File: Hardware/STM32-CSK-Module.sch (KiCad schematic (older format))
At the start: 0 parts

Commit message: Physical interface layout
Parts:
- added H? (x2): CUBESAT-PSPM, ~, symbol CUBESAT-PSPM
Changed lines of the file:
@@
 LIBS:power
 LIBS:Aerodyne_v2
+LIBS:STM32-CSK-Module-cache
 EELAYER 27 0
 EELAYER END
@@
 Comment4 ""
 $EndDescr
+$Comp
+L CUBESAT-PSPM H?
+U 1 1 547E0580
+P 4400 3500
+F 0 "H?" H 4400 4800 60  0000 C CNN
+F 1 "CUBESAT-PSPM" H 4400 2200 60  0000 C CNN
+F 2 "~" H 4400 4100 60  0000 C CNN
+F 3 "~" H 4400 4100 60  0000 C CNN
+	1    4400 3500
+	1    0    0    -1
+$EndComp
+$Comp
+L CUBESAT-PSPM H?
+U 2 1 547E058F
+P 7000 3500
+F 0 "H?" H 7000 4800 60  0000 C CNN
+F 1 "CUBESAT-PSPM" H 7000 2200 60  0000 C CNN
+F 2 "~" H 7000 4100 60  0000 C CNN
+F 3 "~" H 7000 4100 60  0000 C CNN
+	2    7000 3500
+	1    0    0    -1
+$EndComp
 $EndSCHEMATC

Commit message: Annotation
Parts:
- gave numbers to parts that had none: 1
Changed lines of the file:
@@
 $EndDescr
 $Comp
-L CUBESAT-PSPM H?
+L CUBESAT-PSPM H1
 U 1 1 547E0580
 P 4400 3500
-F 0 "H?" H 4400 4800 60  0000 C CNN
+F 0 "H1" H 4400 4800 60  0000 C CNN
 F 1 "CUBESAT-PSPM" H 4400 2200 60  0000 C CNN
 F 2 "~" H 4400 4100 60  0000 C CNN
@@
 $EndComp
 $Comp
-L CUBESAT-PSPM H?
+L CUBESAT-PSPM H1
 U 2 1 547E058F
 P 7000 3500
-F 0 "H?" H 7000 4800 60  0000 C CNN
+F 0 "H1" H 7000 4800 60  0000 C CNN
 F 1 "CUBESAT-PSPM" H 7000 2200 60  0000 C CNN
 F 2 "~" H 7000 4100 60  0000 C CNN

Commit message: Add MCU
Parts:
- added U1: STM32F4X7V, symbol STM32F4X7V
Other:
- note added: "AN0"
- note added: "AN1"
- note added: "AN10"
- note added: "AN11"
- note added: "AN12"
- note added: "AN13"
- note added: "AN14"
- note added: "AN15"
- note added: "AN2"
- note added: "AN3"
- note added: "AN4"
- note added: "AN5"
- note added: "AN6"
- note added: "AN7"
- note added: "AN8"
- note added: "AN9"
- note added: "INT1"
- note added: "INT2"
- note added: "SCK0"
- note added: "SCK1"
- note added: "SCL1"
- note added: "SCL2"
- note added: "SD0"
- note added: "SDA1"
- note added: "SDA2"
- note added: "SDI0"
- note added: "SDI1"
- note added: "SDO1"
- note added: "URX0"
- note added: "URX1"
- note added: "UTX0"
- note added: "UTX1"
- note added: "~CS_SD"
- note added: "~SS1"
- note added: "~UCTS0"
- note added: "~UCTS1"
- note added: "~URTS0"
- note added: "~URTS1"
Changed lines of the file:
@@
 EELAYER 27 0
 EELAYER END
-$Descr A4 11693 8268
+$Descr A3 16535 11693
 encoding utf-8
 Sheet 1 1
 Title ""
-Date "2 dec 2014"
+Date "5 dec 2014"
 Rev ""
 Comp ""
@@
 	1    0    0    -1
 $EndComp
+$Comp
+L STM32F4X7V U1
+U 1 1 54823604
+P 3150 6600
+F 0 "U1" H 3150 6700 60  0000 C CNN
+F 1 "STM32F4X7V" V 2950 6600 60  0000 R CNN
+F 2 "" H 3550 6600 60  0000 C CNN
+F 3 "" H 3550 6600 60  0000 C CNN
+	1    3150 6600
+	1    0    0    -1
+$EndComp
+$Comp
+L STM32F4X7V U1
+U 2 1 54823613
+P 3850 6600
+F 0 "U1" H 3850 6700 60  0000 C CNN
+F 1 "STM32F4X7V" V 3650 6600 60  0000 R CNN
+F 2 "" H 4250 6600 60  0000 C CNN
+F 3 "" H 4250 6600 60  0000 C CNN
+	2    3850 6600
+	1    0    0    -1
+$EndComp
+$Comp
+L STM32F4X7V U1
+U 3 1 54823622
+P 4550 6600
+F 0 "U1" H 4550 6700 60  0000 C CNN
+F 1 "STM32F4X7V" V 4350 6600 60  0000 R CNN
+F 2 "" H 4950 6600 60  0000 C CNN
+F 3 "" H 4950 6600 60  0000 C CNN
+	3    4550 6600
+	1    0    0    -1
+$EndComp
+$Comp
+L STM32F4X7V U1
+U 4 1 54823631
+P 5250 6600
+F 0 "U1" H 5250 6700 60  0000 C CNN
+F 1 "STM32F4X7V" V 5050 6600 60  0000 R CNN
+F 2 "" H 5650 6600 60  0000 C CNN
+F 3 "" H 5650 6600 60  0000 C CNN
+	4    5250 6600
+	1    0    0    -1
+$EndComp
+$Comp
+L STM32F4X7V U1
+U 5 1 54823640
+P 5950 6600
+F 0 "U1" H 5950 6700 60  0000 C CNN
+F 1 "STM32F4X7V" V 5750 6600 60  0000 R CNN
+F 2 "" H 6350 6600 60  0000 C CNN
+F 3 "" H 6350 6600 60  0000 C CNN
+	5    5950 6600
+	1    0    0    -1
+$EndComp
+$Comp
+L STM32F4X7V U1
+U 6 1 54823663
+P 6650 6600
+F 0 "U1" H 6650 6700 60  0000 C CNN
+F 1 "STM32F4X7V" V 6450 6600 60  0000 R CNN
+F 2 "" H 7050 6600 60  0000 C CNN
+F 3 "" H 7050 6600 60  0000 C CNN
+	6    6650 6600
+	1    0    0    -1
+$EndComp
+$Comp
+L STM32F4X7V U1
+U 7 1 54823677
+P 7350 6600
+F 0 "U1" H 7350 6700 60  0000 C CNN
+F 1 "STM32F4X7V" V 7150 6600 60  0000 R CNN
+F 2 "" H 7750 6600 60  0000 C CNN
+F 3 "" H 7750 6600 60  0000 C CNN
+	7    7350 6600
+	1    0    0    -1
+$EndComp
+$Comp
+L STM32F4X7V U1
+U 8 1 5482368B
+P 8050 6600
+F 0 "U1" H 8050 6700 60  0000 C CNN
+F 1 "STM32F4X7V" V 7850 6600 60  0000 R CNN
+F 2 "" H 8450 6600 60  0000 C CNN
+F 3 "" H 8450 6600 60  0000 C CNN
+	8    8050 6600
+	1    0    0    -1
+$EndComp
+Text Notes 3800 4600 2    60   ~ 0
+~CS_SD
+Text Notes 3800 4500 2    60   ~ 0
+SD0
+Text Notes 3800 4400 2    60   ~ 0
+SDI0
+Text Notes 3800 4300 2    60   ~ 0
+SCK0
+Text Notes 3800 4200 2    60   ~ 0
+UTX0
+Text Notes 3800 4100 2    60   ~ 0
+URX0
+Text Notes 3800 4000 2    60   ~ 0
+UTX1
+Text Notes 3800 3900 2    60   ~ 0
+URX1
+Text Notes 3800 3800 2    60   ~ 0
+~SS1
+Text Notes 3800 3700 2    60   ~ 0
+SDO1
+Text Notes 3800 3600 2    60   ~ 0
+SDI1
+Text Notes 3800 3500 2    60   ~ 0
+SCK1
+Text Notes 3800 3400 2    60   ~ 0
+~URTS0
+Text Notes 3800 3300 2    60   ~ 0
+~UCTS0
+Text Notes 3800 3200 2    60   ~ 0
+~URTS1
+Text Notes 3800 3100 2    60   ~ 0
+~UCTS1
+Text Notes 3800 2600 2    60   ~ 0
+SCL1
+Text Notes 3800 2500 2    60   ~ 0
+SDA1
+Text Notes 3800 2400 2    60   ~ 0
+SCL2
+Text Notes 3800 2300 2    60   ~ 0
+SDA2
+Text Notes 5000 4000 0    60   ~ 0
+INT1
+Text Notes 5000 3900 0    60   ~ 0
+INT2
+Text Notes 5000 3800 0    60   ~ 0
+AN8
+Text Notes 5000 3700 0    60   ~ 0
+AN9
+Text Notes 5000 3600 0    60   ~ 0
+AN10
+Text Notes 5000 3500 0    60   ~ 0
+AN11
+Text Notes 5000 3400 0    60   ~ 0
+AN12
+Text Notes 5000 3300 0    60   ~ 0
+AN13
+Text Notes 5000 3200 0    60   ~ 0
+AN14
+Text Notes 5000 3100 0    60   ~ 0
+AN15
+Text Notes 5000 3000 0    60   ~ 0
+AN0
+Text Notes 5000 2900 0    60   ~ 0
+AN1
+Text Notes 5000 2800 0    60   ~ 0
+AN2
+Text Notes 5000 2700 0    60   ~ 0
+AN3
+Text Notes 5000 2600 0    60   ~ 0
+AN4
+Text Notes 5000 2500 0    60   ~ 0
+AN5
+Text Notes 5000 2400 0    60   ~ 0
+AN6
+Text Notes 5000 2300 0    60   ~ 0
+AN7
 $EndSCHEMATC

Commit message: Migrate to new KiCad
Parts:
- removed H1: CUBESAT-PSPM, ~, symbol CUBESAT-PSPM
- removed U1: STM32F4X7V, symbol STM32F4X7V
- added C1, C10, C12, C13, C2, C5, C6, C7, C8: 0.1uF, Capacitors:CAPC1608N, symbol Capacitor
- added C11, C9: 2.2uF, Capacitors:CAPC1608N, symbol Capacitor
- added C3: 1uF, Capacitors:CAPC1608N, symbol Capacitor
- added C4: 4.7uF, Capacitors:CAPC1608N, symbol Capacitor
- added FB1: Ferrite, Inductors:INDC1608N, symbol Ferrite
- added H1: Conn_Cubesat-PPM, Connectors:Conn_Samtec-LSS-150, symbol Conn_Cubesat-PPM
- added R1: 10k, Resistors:RESC1608N, symbol Resistor
- added U1: STM32F417VGT, QFP:QFP50P1600X1600-100N, symbol STM32F417VGT
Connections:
- net labels added: +3V3, BOOT, GND, VBAT, VCAP1, VCAP2, VDD, VDDA, ~RST
- wire segments 0 -> 52
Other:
- note removed: "AN0"
- note removed: "AN1"
- note removed: "AN10"
- note removed: "AN11"
- note removed: "AN12"
- note removed: "AN13"
- note removed: "AN14"
- note removed: "AN15"
- note removed: "AN2"
- note removed: "AN3"
- note removed: "AN4"
- note removed: "AN5"
- note removed: "AN6"
- note removed: "AN7"
- note removed: "AN8"
- note removed: "AN9"
- note removed: "INT1"
- note removed: "INT2"
- note removed: "SCK0"
- note removed: "SCK1"
- note removed: "SCL1"
- note removed: "SCL2"
- note removed: "SD0"
- note removed: "SDA1"
- note removed: "SDA2"
- note removed: "SDI0"
- note removed: "SDI1"
- note removed: "SDO1"
- note removed: "URX0"
- note removed: "URX1"
- note removed: "UTX0"
- note removed: "UTX1"
- note removed: "~CS_SD"
- note removed: "~SS1"
- note removed: "~UCTS0"
- note removed: "~UCTS1"
- note removed: "~URTS0"
- note removed: "~URTS1"

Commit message: Add crystals and programmer
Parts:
- added C? (x4): Capacitor, symbol Capacitor
- added J1: Conn_Cortex-JTAG-10, Connectors:Conn_Samtec-FTSH-105-D-RA-K, symbol Conn_Cortex-JTAG-10
- added X?: 8MHz, symbol Crystal
- added X?: 32.768kHz, symbol Crystal
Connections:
- net +3V3: now also J1.1 (VT)
- net GND: now also C?.2, C?.2, C?.2, C?.2, J1.3 (GND), J1.5 (GND), J1.9 (DET)
- net ~RST: now also J1.10 (~RESET)
- net SWDIO: now reaches U1.72 (PA13)
- net SWDIO: now also J1.2 (SWDIO/TMS)
- net SWCLK: now reaches U1.76 (PA14)
- net SWCLK: now also J1.4 (SWCLK/TCK)
- net SOSCI: now reaches U1.8 (PC14)
- net SOSCI: now also C?.1, X?.1
- net SOSCO: now reaches U1.9 (PC15)
- net SOSCO: now also C?.1, X?.2
- net OSCI: now reaches U1.12 (PH0)
- net OSCI: now also C?.1, X?.1
- net OSCO: now reaches U1.13 (PH1)
- net OSCO: now also C?.1, X?.2
- no-connect marks 0 -> 2
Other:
- moved on the sheet: U1A, U1C

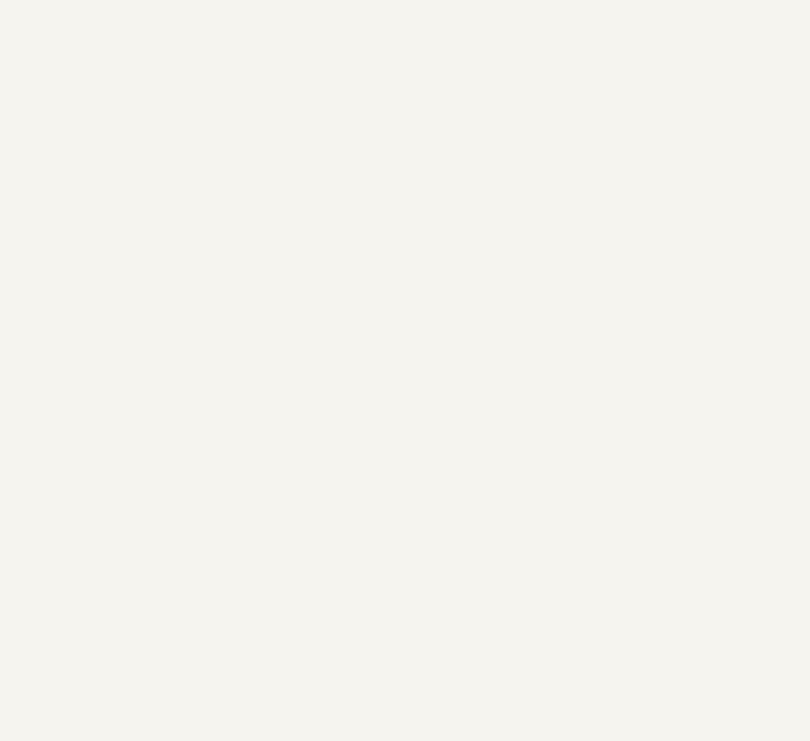
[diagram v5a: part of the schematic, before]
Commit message: Add flash
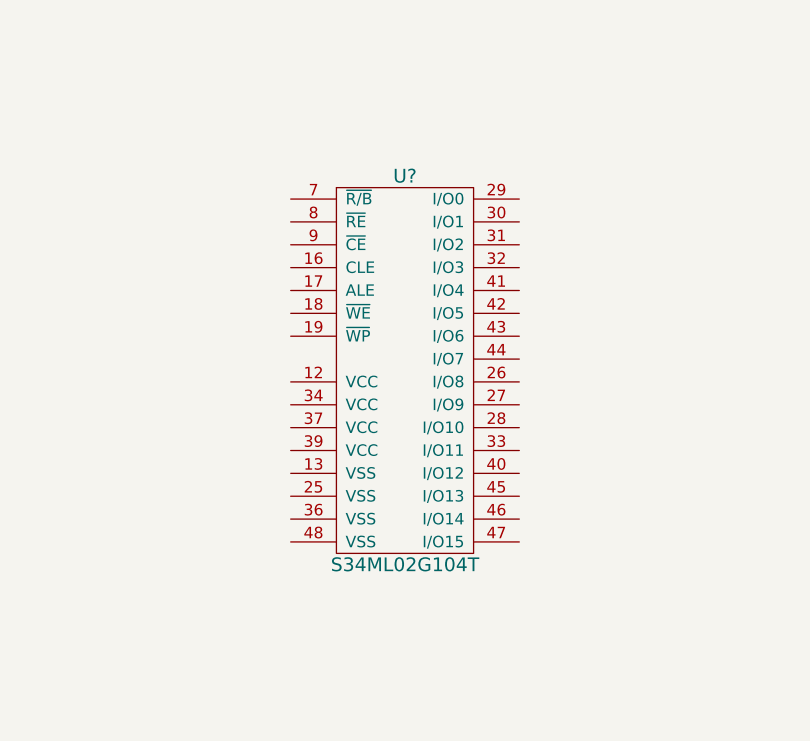
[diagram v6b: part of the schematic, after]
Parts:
- added U?: S34ML02G104T, symbol S34ML02G104T
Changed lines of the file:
@@
 LIBS:Passives
 LIBS:STMicroelectronics
+LIBS:Microchip
 LIBS:STM32-CSK-Module-cache
 EELAYER 25 0
@@
 	6900 9800 6900 9700
 Connection ~ 6900 9700
+$Comp
+L S34ML02G104T U?
+U 1 1 54B6F9F3
+P 10300 7750
+F 0 "U?" H 10300 8600 60  0000 C CNN
+F 1 "S34ML02G104T" H 10300 6900 60  0000 C CNN
+F 2 "" H 10300 7600 60  0000 C CNN
+F 3 "" H 10300 7600 60  0000 C CNN
+F 4 "Spansion" H 10300 7750 60  0001 C CNN "Manufacturer"
+F 5 "S34ML02G104TFI010" H 10300 7750 60  0001 C CNN "Manufacturer Part #"
+F 6 "Datasheet" H 10300 7750 60  0001 C CNN "Vendor"
+F 7 "1274-1090-ND" H 10300 7750 60  0001 C CNN "Vendor Part #"
+	1    10300 7750
+	1    0    0    -1
+$EndComp
 $EndSCHEMATC

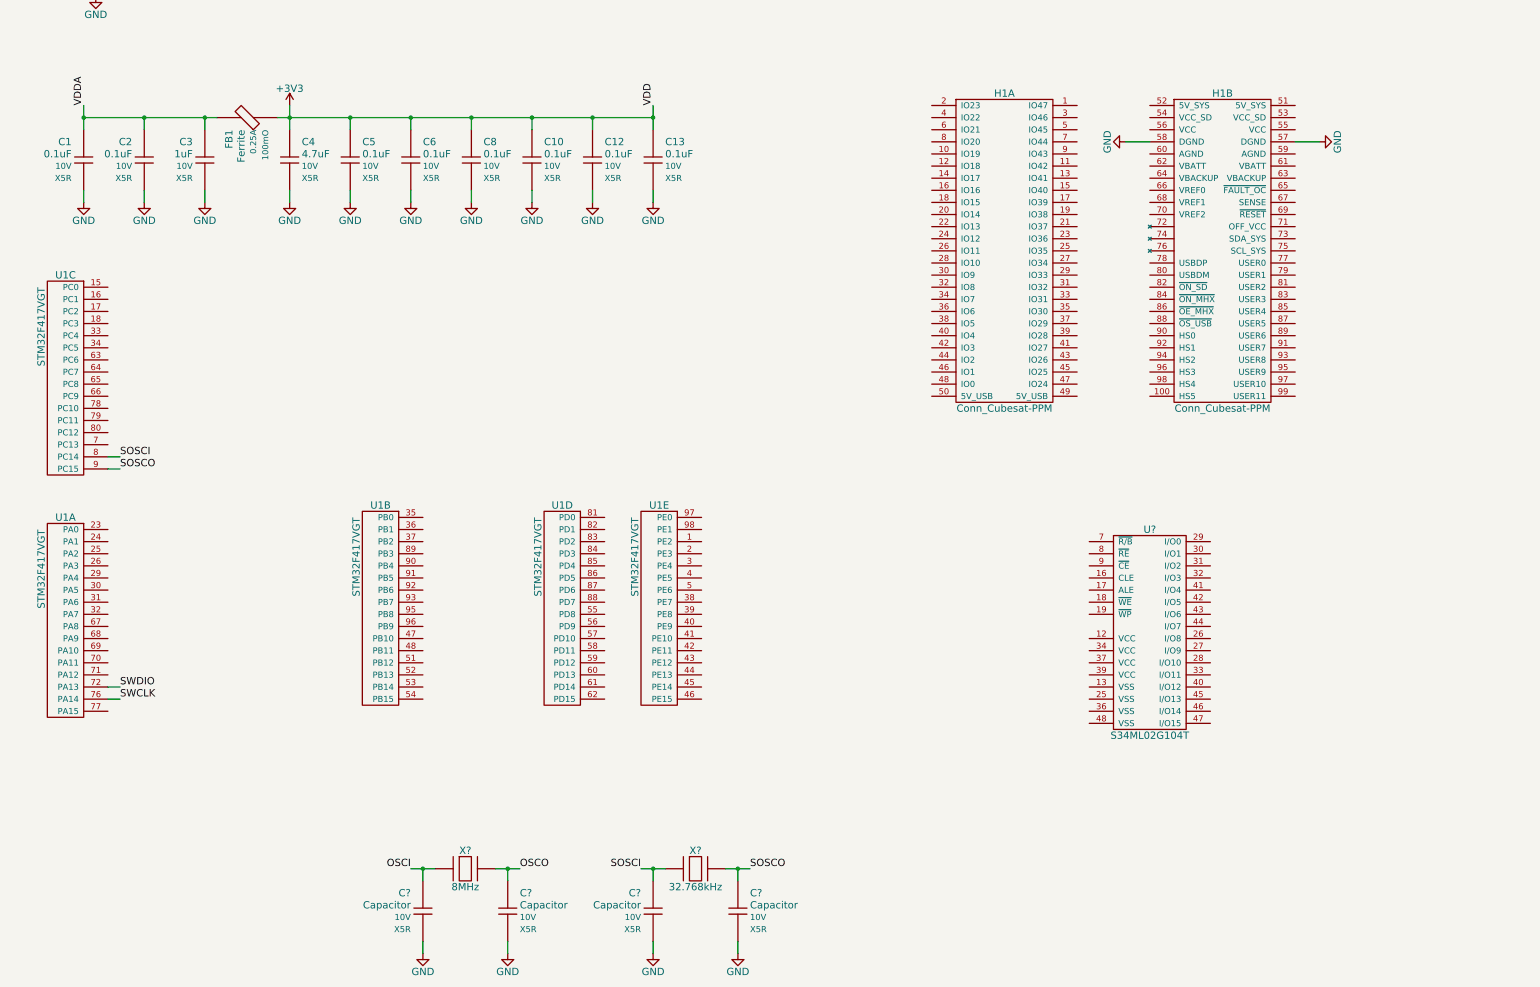
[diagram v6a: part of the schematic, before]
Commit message: Peripheral pin mapping
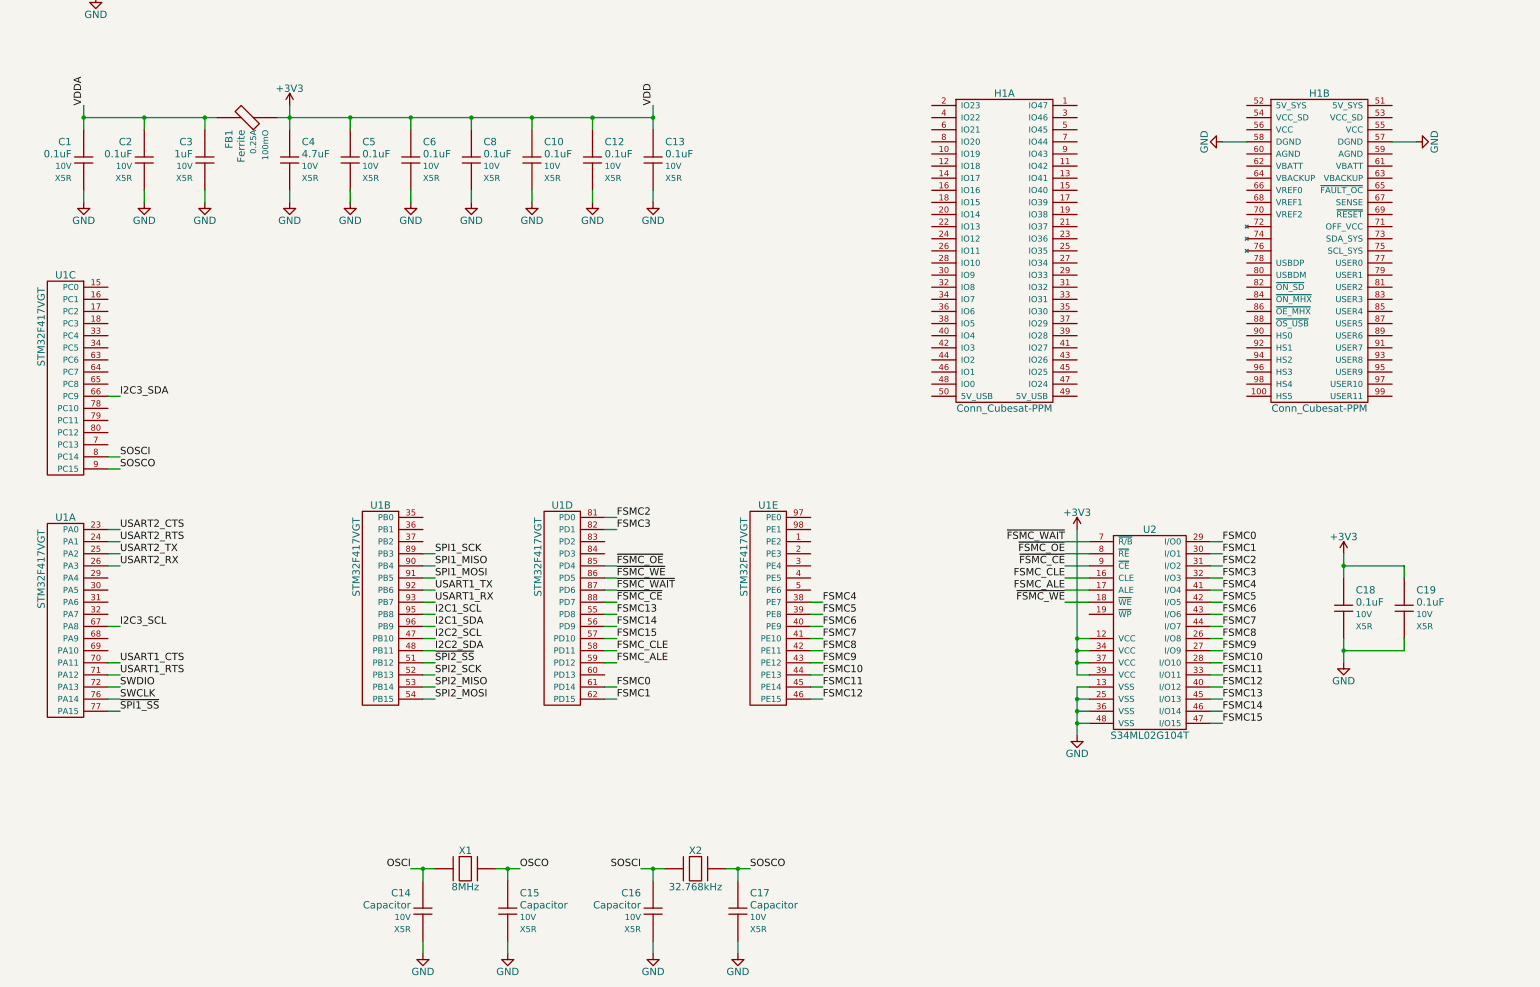
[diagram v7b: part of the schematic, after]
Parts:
- added C18, C19: 0.1uF, Capacitors:CAPC1608N, symbol Capacitor
- U2: renamed from U?; footprint (none) -> SOP:SOP50P2000-48N
- gave numbers to parts that had none: 6
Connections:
- net +3V3: now also U2.12 (VCC), U2.34 (VCC), U2.37 (VCC), U2.39 (VCC), C18.1, C19.1
- net GND: now also U2.13 (VSS), U2.25 (VSS), U2.36 (VSS), U2.48 (VSS), C18.2, C19.2
- net USART2_CTS: now reaches U1.23 (PA0)
- net USART2_RTS: now reaches U1.24 (PA1)
- net USART2_TX: now reaches U1.25 (PA2)
- net USART2_RX: now reaches U1.26 (PA3)
- net I2C3_SCL: now reaches U1.67 (PA8)
- net USART1_CTS: now reaches U1.70 (PA11)
- net USART1_RTS: now reaches U1.71 (PA12)
- net ~SPI1_SS: now reaches U1.77 (PA15)
- net I2C2_SCL: now reaches U1.47 (PB10)
- net I2C2_SDA: now reaches U1.48 (PB11)
- net ~SPI2_SS: now reaches U1.51 (PB12)
- net SPI2_SCK: now reaches U1.52 (PB13)
- net SPI2_MISO: now reaches U1.53 (PB14)
- net SPI2_MOSI: now reaches U1.54 (PB15)
- net SPI1_SCK: now reaches U1.89 (PB3)
- net SPI1_MISO: now reaches U1.90 (PB4)
- net SPI1_MOSI: now reaches U1.91 (PB5)
- net USART1_TX: now reaches U1.92 (PB6)
- net USART1_RX: now reaches U1.93 (PB7)
- net I2C1_SCL: now reaches U1.95 (PB8)
- net I2C1_SDA: now reaches U1.96 (PB9)
- net I2C3_SDA: now reaches U1.66 (PC9)
- net FSMC13: now reaches U1.55 (PD8)
- net FSMC13: now also U2.45 (I/O13)
- net FSMC14: now reaches U1.56 (PD9)
- net FSMC14: now also U2.46 (I/O14)
- net FSMC15: now reaches U1.57 (PD10)
- net FSMC15: now also U2.47 (I/O15)
- net FSMC_CLE: now reaches U1.58 (PD11)
- net FSMC_CLE: now also U2.16 (CLE)
- net FSMC_ALE: now reaches U1.59 (PD12)
- net FSMC_ALE: now also U2.17 (ALE)
- net FSMC0: now reaches U1.61 (PD14)
- net FSMC0: now also U2.29 (I/O0)
- net FSMC1: now reaches U1.62 (PD15)
- net FSMC1: now also U2.30 (I/O1)
- net FSMC2: now reaches U1.81 (PD0)
- net FSMC2: now also U2.31 (I/O2)
- net FSMC3: now reaches U1.82 (PD1)
- net FSMC3: now also U2.32 (I/O3)
- net ~FSMC_OE: now reaches U1.85 (PD4)
- net ~FSMC_OE: now also U2.8 (~RE)
- net ~FSMC_WE: now reaches U1.86 (PD5)
- net ~FSMC_WE: now also U2.18 (~WE)
- net ~FSMC_WAIT: now reaches U1.87 (PD6)
- net ~FSMC_WAIT: now also U2.7 (~R/B)
- net ~FSMC_CE: now reaches U1.88 (PD7)
- net ~FSMC_CE: now also U2.9 (~CE)
- net FSMC4: now reaches U1.38 (PE7)
- net FSMC4: now also U2.41 (I/O4)
- net FSMC5: now reaches U1.39 (PE8)
- net FSMC5: now also U2.42 (I/O5)
- net FSMC6: now reaches U1.40 (PE9)
- net FSMC6: now also U2.43 (I/O6)
- net FSMC7: now reaches U1.41 (PE10)
- net FSMC7: now also U2.44 (I/O7)
- net FSMC8: now reaches U1.42 (PE11)
- net FSMC8: now also U2.26 (I/O8)
- net FSMC9: now reaches U1.43 (PE12)
- net FSMC9: now also U2.27 (I/O9)
- net FSMC10: now reaches U1.44 (PE13)
- net FSMC10: now also U2.28 (I/O10)
- net FSMC11: now reaches U1.45 (PE14)
- net FSMC11: now also U2.33 (I/O11)
- net FSMC12: now reaches U1.46 (PE15)
- net FSMC12: now also U2.40 (I/O12)
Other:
- moved on the sheet: H1B, U1E

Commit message: Peripheral PPM connections
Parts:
- added R2, R3: 0, Resistors:RESC1608N, symbol Resistor
- C14, C15, C16, C17: footprint (none) -> Capacitors:CAPC1608N
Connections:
- net +3V3: now also H1.55 (VCC), H1.56 (VCC)
- net GND: now also R3.1
- net I2C1_SCL: now also H1.75 (SCL_SYS)
- net I2C1_SDA: now also H1.73 (SDA_SYS)
- net I2C2_SCL: now also H1.8 (IO20)
- net I2C2_SDA: now also H1.6 (IO21)
- net I2C3_SCL: now also H1.4 (IO22)
- net I2C3_SDA: now also H1.2 (IO23)
- net SPI1_MISO: now also H1.44 (IO2)
- net SPI1_MOSI: now also H1.46 (IO1)
- net SPI1_SCK: now also H1.42 (IO3)
- net SPI2_MISO: now also H1.28 (IO10)
- net SPI2_MOSI: now also H1.30 (IO9)
- net SPI2_SCK: now also H1.26 (IO11)
- net USART1_CTS: now also H1.18 (IO15)
- net USART1_RTS: now also H1.20 (IO14)
- net USART1_RX: now also H1.34 (IO7)
- net USART1_TX: now also H1.36 (IO6)
- net USART2_CTS: now also H1.22 (IO13)
- net USART2_RTS: now also H1.24 (IO12)
- net USART2_RX: now also H1.38 (IO5)
- net USART2_TX: now also H1.40 (IO4)
- net VDDA: now also R2.2; no longer C1.1, U1.21 (VREF+)
- net ~SPI1_SS: now also H1.48 (IO0)
- net ~SPI2_SS: now also H1.32 (IO8)
- net ~FSMC_WP: now reaches U1.60 (PD13)
- net ~FSMC_WP: now also U2.19 (~WP)
- net GNDA: now reaches H1.59 (AGND)
- net GNDA: now also H1.60 (AGND), R3.2
- net VREF: now reaches H1.66 (VREF0)
- net VREF: now also C1.1, U1.21 (VREF+), R2.1
- net ~RESET: now reaches H1.69 (~RESET)
- net ~ON_SD: now reaches H1.82 (~ON_SD)
- no-connect marks 2 -> 40
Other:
- note added: "A"
- note added: "I"
- moved on the sheet: C1
